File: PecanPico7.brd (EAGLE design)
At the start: 34.2 x 50 mm, 153 parts, among them IC1 Si4464-B1B-FM, IC10 TC1185-1.8VCT713, IC11 TC1185-2.5VCT713, IC12 ADR380ARTZ, IC13 RF6886, IC2 Si4464-B1B-FM, IC3 BME280_BME280, IC4 UBLOX_MAX-6, IC5 STM32F429IIH6, IC7 SPV1040, IC8 TXC_7Z, IC9 TPS62260DRVT, Q1 AP2301, Q2 AP2301, Q3 AP2301, U1 USD-SOCKETUSD, U2 PAC1720-1-AIA-TR, X1 CAMERA_HEADER

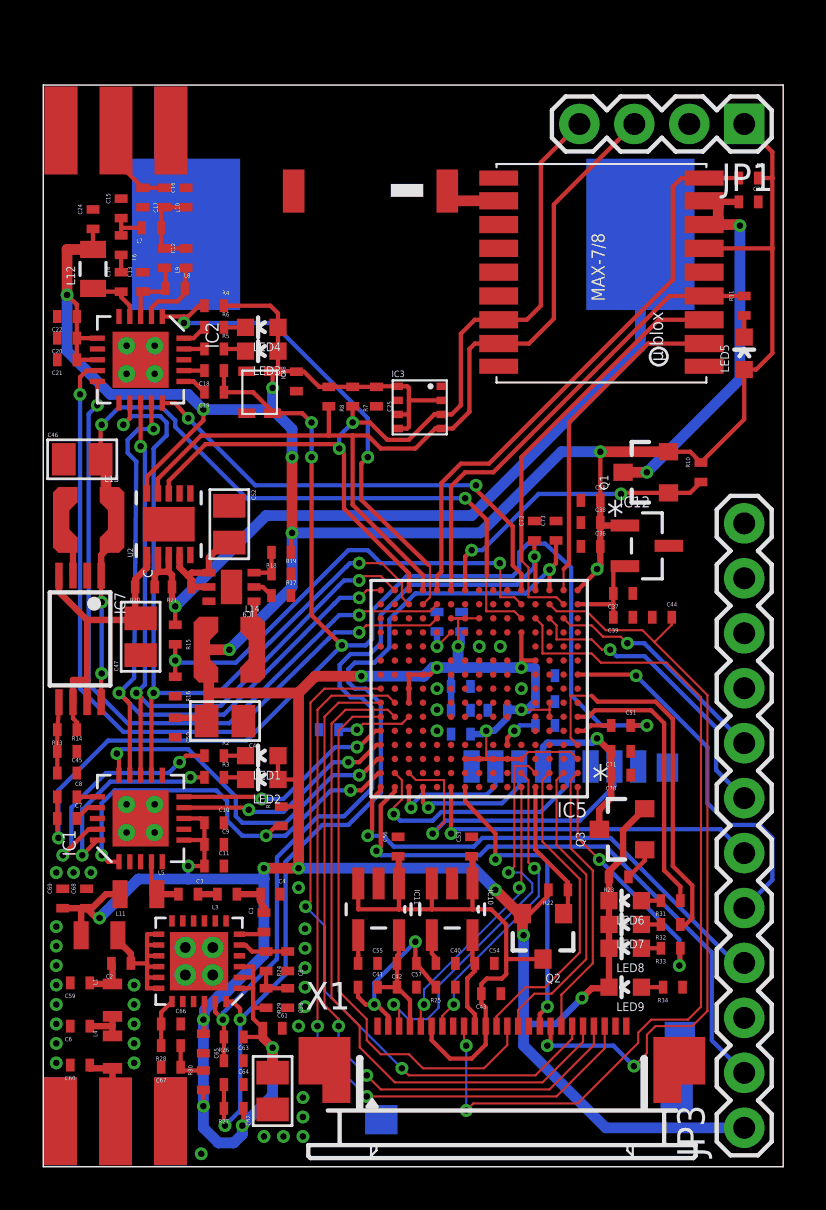
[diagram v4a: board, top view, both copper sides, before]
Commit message: Connected LED pins to pinheader
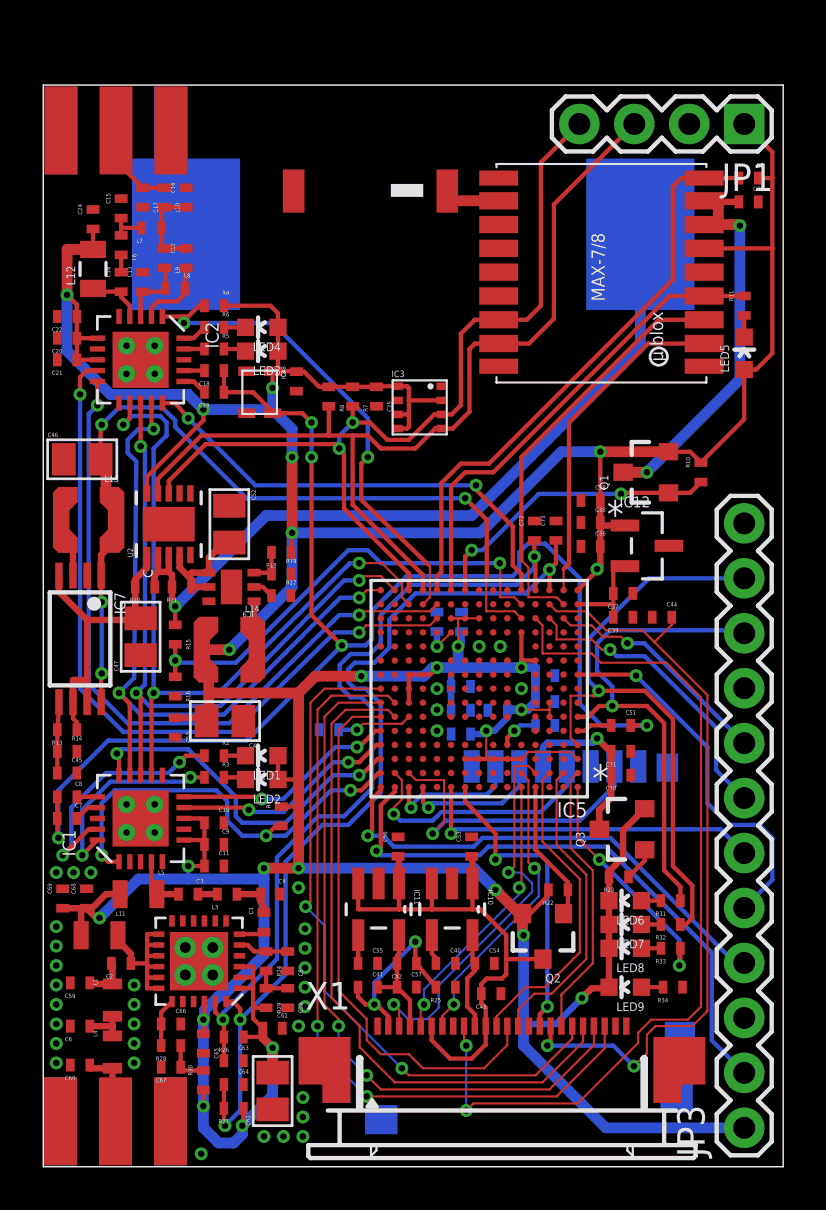
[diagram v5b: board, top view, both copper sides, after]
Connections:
- removed net N$45: JP3.10
- removed net N$46: JP3.11
- net LED1: now also JP3.10
- net LED2: now also JP3.11
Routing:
- net LED2: track 17.8 -> 29.0 mm, vias 0 -> 1
- net LED1: track 12.9 -> 23.3 mm, vias 0 -> 1
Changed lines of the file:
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@@
 <wire x1="15.2" y1="24.4" x2="14.9" y2="24.1" width="0.2" layer="16"/>
 <wire x1="14.9" y1="24.1" x2="13.8" y2="24.1" width="0.2" layer="16"/>
-<wire x1="23.2" y1="28.8" x2="24.4" y2="27.7" width="0.2" layer="16"/>
-<wire x1="24.4" y1="27.7" x2="24.4" y2="21.8" width="0.2" layer="16"/>
-<wire x1="24.4" y1="21.8" x2="25.8" y2="20.4" width="0.2" layer="16"/>
+<wire x1="23.2" y1="28.8" x2="24.8" y2="27.2" width="0.2" layer="16"/>
+<wire x1="24.8" y1="27.2" x2="24.8" y2="21.4" width="0.2" layer="16"/>
+<wire x1="24.8" y1="21.4" x2="25.8" y2="20.4" width="0.2" layer="16"/>
 <wire x1="25.8" y1="20.4" x2="27.9" y2="20.4" width="0.2" layer="16"/>
 <wire x1="27.15" y1="20.4" x2="27.9" y2="20.4" width="0.2" layer="1"/>
@@
 <contactref element="R24" pad="P$2"/>
 <contactref element="C5" pad="P$2"/>
-<wire x1="9.064" y1="10.25" x2="9.35" y2="10.25" width="0.2" layer="1"/>
-<wire x1="9.35" y1="10.25" x2="9.65" y2="9.95" width="0.2" layer="1"/>
-<wire x1="9.65" y1="9.95" x2="10.3" y2="9.95" width="0.2" layer="1"/>
+<wire x1="9.064" y1="10.25" x2="9.45" y2="10.25" width="0.2" layer="1"/>
+<wire x1="9.45" y1="10.25" x2="9.75" y2="9.95" width="0.2" layer="1"/>
+<wire x1="9.75" y1="9.95" x2="10.3" y2="9.95" width="0.2" layer="1"/>
 <wire x1="10.3" y1="9.95" x2="11.3" y2="9.95" width="0.2" layer="1"/>
 </signal>
@@
 <wire x1="21.2" y1="8.7" x2="21.4" y2="8.9" width="0.2" layer="1"/>
 <wire x1="21.4" y1="8.9" x2="21.4" y2="9.6" width="0.2" layer="1"/>
-<wire x1="21.4" y1="9.6" x2="21.4" y2="11.2" width="0.2" layer="1"/>
-<wire x1="21.4" y1="11.2" x2="20.7" y2="11.9" width="0.2" layer="1"/>
+<wire x1="21.4" y1="9.6" x2="21.4" y2="10.7" width="0.2" layer="1"/>
+<wire x1="21.4" y1="10.7" x2="20.2" y2="11.9" width="0.2" layer="1"/>
 <wire x1="14.5602" y1="13.0938" x2="14.5602" y2="11.9" width="0.2" layer="1"/>
 <wire x1="14.5602" y1="11.9" x2="16.4398" y2="11.9" width="0.2" layer="1"/>
 <wire x1="16.4398" y1="11.9" x2="17.9602" y2="11.9" width="0.2" layer="1"/>
 <wire x1="17.9602" y1="11.9" x2="19.8398" y2="11.9" width="0.2" layer="1"/>
-<wire x1="19.8398" y1="11.9" x2="20.7" y2="11.9" width="0.2" layer="1"/>
+<wire x1="19.8398" y1="11.9" x2="20.2" y2="11.9" width="0.2" layer="1"/>
 <wire x1="16.4398" y1="13.0938" x2="16.4398" y2="11.9" width="0.2" layer="1"/>
 <wire x1="17.9602" y1="13.0938" x2="17.9602" y2="11.9" width="0.2" layer="1"/>
@@
 <wire x1="27.8" y1="14.15" x2="27.8" y2="14.65" width="0.2" layer="1"/>
 </signal>
-<signal name="N$45">
-<contactref element="JP3" pad="10"/>
-</signal>
-<signal name="N$46">
-<contactref element="JP3" pad="11"/>
-</signal>
 <signal name="UART_TXD">
 <contactref element="IC5" pad="N3"/>
@@
 <wire x1="24.7" y1="19.5" x2="24.375" y2="19.825" width="0.1" layer="1"/>
 <wire x1="24.375" y1="19.825" x2="24.375" y2="21.775" width="0.1" layer="1"/>
-<wire x1="24.375" y1="21.775" x2="25.35" y2="21.775" width="0.1" layer="1"/>
-<wire x1="25.35" y1="21.775" x2="25.625" y2="21.5" width="0.2" layer="1"/>
-<wire x1="25.625" y1="21.5" x2="28.3" y2="21.5" width="0.2" layer="1"/>
-<wire x1="28.3" y1="21.5" x2="29.1" y2="20.7" width="0.2" layer="1"/>
+<wire x1="24.375" y1="21.775" x2="25.45" y2="21.775" width="0.1" layer="1"/>
+<wire x1="27.8" y1="22" x2="29.1" y2="20.7" width="0.2" layer="1"/>
 <wire x1="29.1" y1="20.7" x2="29.1" y2="13.9" width="0.2" layer="1"/>
 <wire x1="29.1" y1="13.9" x2="30" y2="13" width="0.2" layer="1"/>
@@
 <wire x1="30" y1="11.5" x2="29.7" y2="11.2" width="0.2" layer="1"/>
 <wire x1="29.7" y1="11.2" x2="29.45" y2="11.2" width="0.2" layer="1"/>
+<wire x1="25.675" y1="22" x2="25.45" y2="21.775" width="0.2" layer="1"/>
+<contactref element="JP3" pad="11"/>
+<via x="25.675" y="22" extent="1-16" drill="0.3"/>
+<wire x1="27.8" y1="22" x2="25.675" y2="22" width="0.2" layer="1"/>
+<wire x1="25.675" y1="22" x2="25.2" y2="22.475" width="0.2" layer="16"/>
+<wire x1="25.2" y1="22.475" x2="25.2" y2="24.4" width="0.2" layer="16"/>
+<wire x1="25.2" y1="24.4" x2="28" y2="27.2" width="0.2" layer="16"/>
+<wire x1="28" y1="27.2" x2="32.4" y2="27.2" width="0.2" layer="16"/>
 </signal>
 <signal name="LED1">
@@
 <contactref element="IC5" pad="F1"/>
 <wire x1="24.7" y1="20.8" x2="25.2" y2="20.8" width="0.2" layer="1"/>
-<wire x1="25.2" y1="20.8" x2="25.5" y2="21.1" width="0.2" layer="1"/>
-<wire x1="25.5" y1="21.1" x2="28.1" y2="21.1" width="0.2" layer="1"/>
-<wire x1="28.1" y1="21.1" x2="28.7" y2="20.5" width="0.2" layer="1"/>
+<wire x1="25.2" y1="20.8" x2="25.7" y2="21.3" width="0.2" layer="1"/>
+<wire x1="27.9" y1="21.3" x2="28.7" y2="20.5" width="0.2" layer="1"/>
 <wire x1="28.7" y1="20.5" x2="28.7" y2="13.7" width="0.2" layer="1"/>
 <wire x1="28.7" y1="13.7" x2="29.45" y2="12.95" width="0.2" layer="1"/>
 <wire x1="29.45" y1="12.95" x2="29.45" y2="12.3" width="0.2" layer="1"/>
+<contactref element="JP3" pad="10"/>
+<via x="26.3" y="21.3" extent="1-16" drill="0.3"/>
+<wire x1="25.7" y1="21.3" x2="26.3" y2="21.3" width="0.2" layer="1"/>
+<wire x1="27.9" y1="21.3" x2="26.3" y2="21.3" width="0.2" layer="1"/>
+<wire x1="26.3" y1="21.3" x2="26.3" y2="22.2" width="0.2" layer="16"/>
+<wire x1="26.3" y1="22.2" x2="25.6" y2="22.9" width="0.2" layer="16"/>
+<wire x1="25.6" y1="22.9" x2="25.6" y2="24.2" width="0.2" layer="16"/>
+<wire x1="25.6" y1="24.2" x2="26.2" y2="24.8" width="0.2" layer="16"/>
+<wire x1="26.2" y1="24.8" x2="32.26" y2="24.8" width="0.2" layer="16"/>
+<wire x1="32.26" y1="24.8" x2="32.4" y2="24.66" width="0.2" layer="16"/>
 </signal>
 <signal name="LED3">

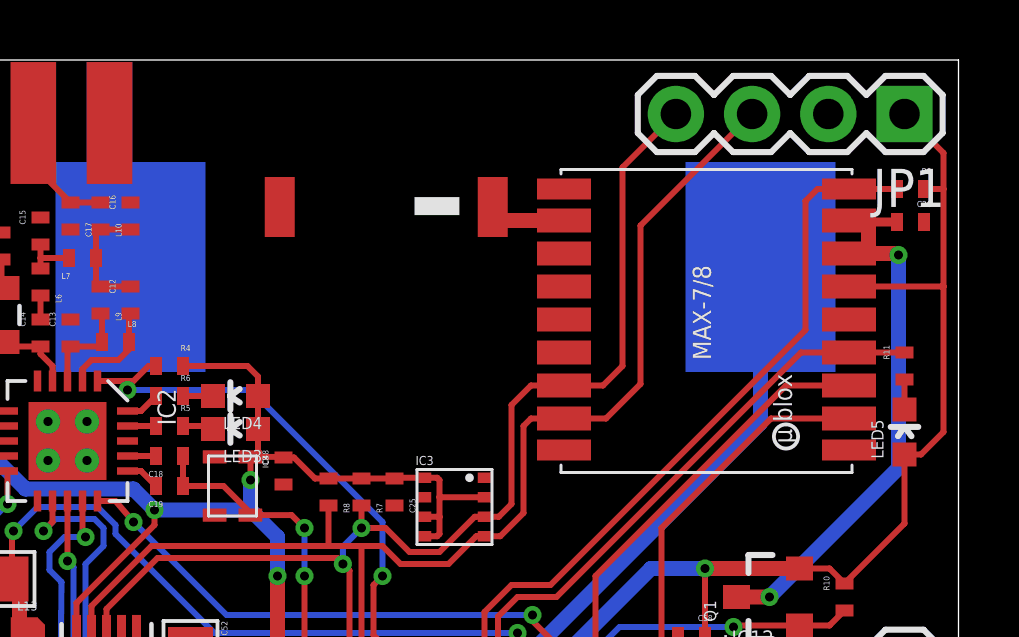
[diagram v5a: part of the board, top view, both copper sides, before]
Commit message: Added GPS preamplifier
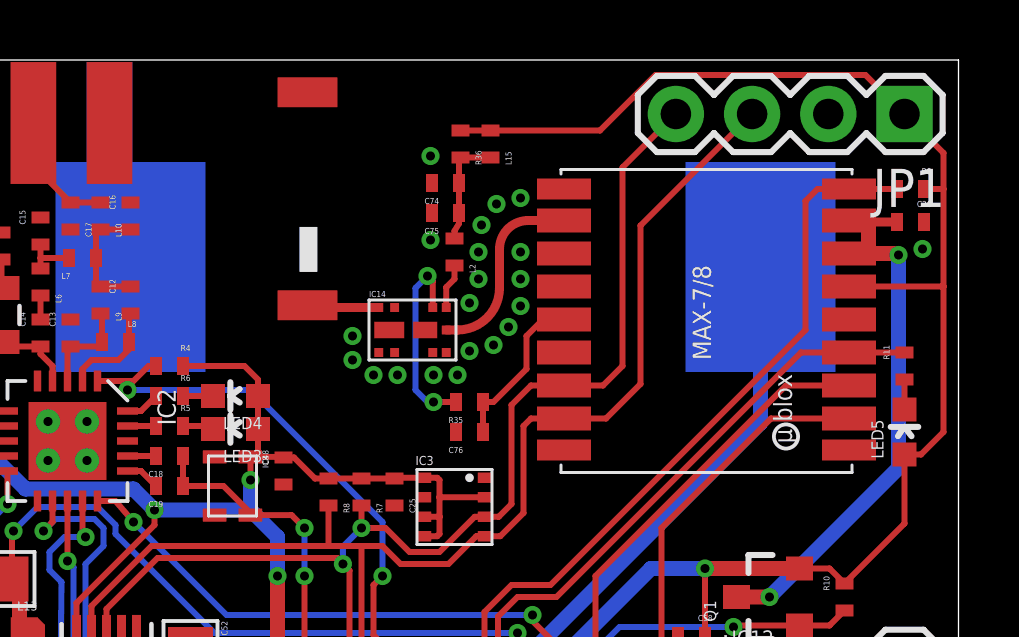
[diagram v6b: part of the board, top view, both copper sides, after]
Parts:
- added C74, C75, C76, L15, L2, R35, R36: (no value), PecanPico6:0402
- added IC14: ALM-GP003, stm32f42x:ALM-GP003
- C25: value 100pF -> 100nF
- R11: value 10k -> 3.3k
- moved U$4 3.00 mm to (12.5, 45.0), turned to 90 degrees
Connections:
- new net GPS_BIAS: C76.P$2, IC4.14_VCC_RF, R35.P$2
- new net N$45: IC14.8, R35.P$1
- new net N$46: IC14.7, L2.P$1
- new net N$51: C74.P$2, C75.P$2, L15.P$1, L2.P$2, R36.P$1
- new net N$7: IC14.1, U$4.FEED
- net GND: now also C74.P$1, C75.P$1, C76.P$1, IC14.2, IC14.3, IC14.4, IC14.9, IC14.P1, IC14.P2
- net N$33: now also IC14.6; no longer U$4.FEED
- net VCC: now also L15.P$2, R36.P$2
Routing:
- net VCC: track 268.2 -> 284.3 mm
- net N$45: track 0.00 -> 6.60 mm, vias 0 -> 2
- net GPS_BIAS: track 0.00 -> 5.48 mm
- net N$51: track 0.00 -> 3.79 mm
- net N$33: track 2.83 -> 6.20 mm
- net N$7: track 0.00 -> 2.45 mm
- net N$46: track 0.00 -> 1.51 mm

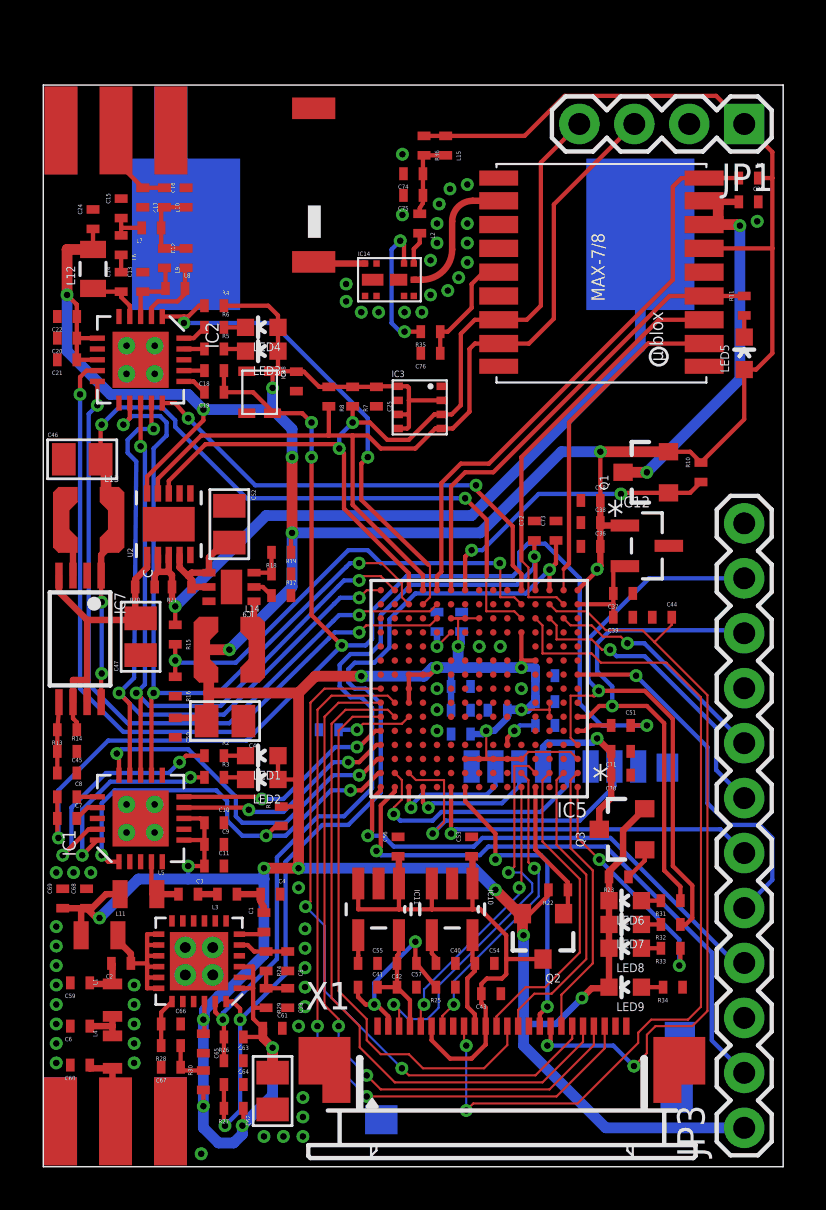
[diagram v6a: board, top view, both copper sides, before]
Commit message: Fixed impedance errors
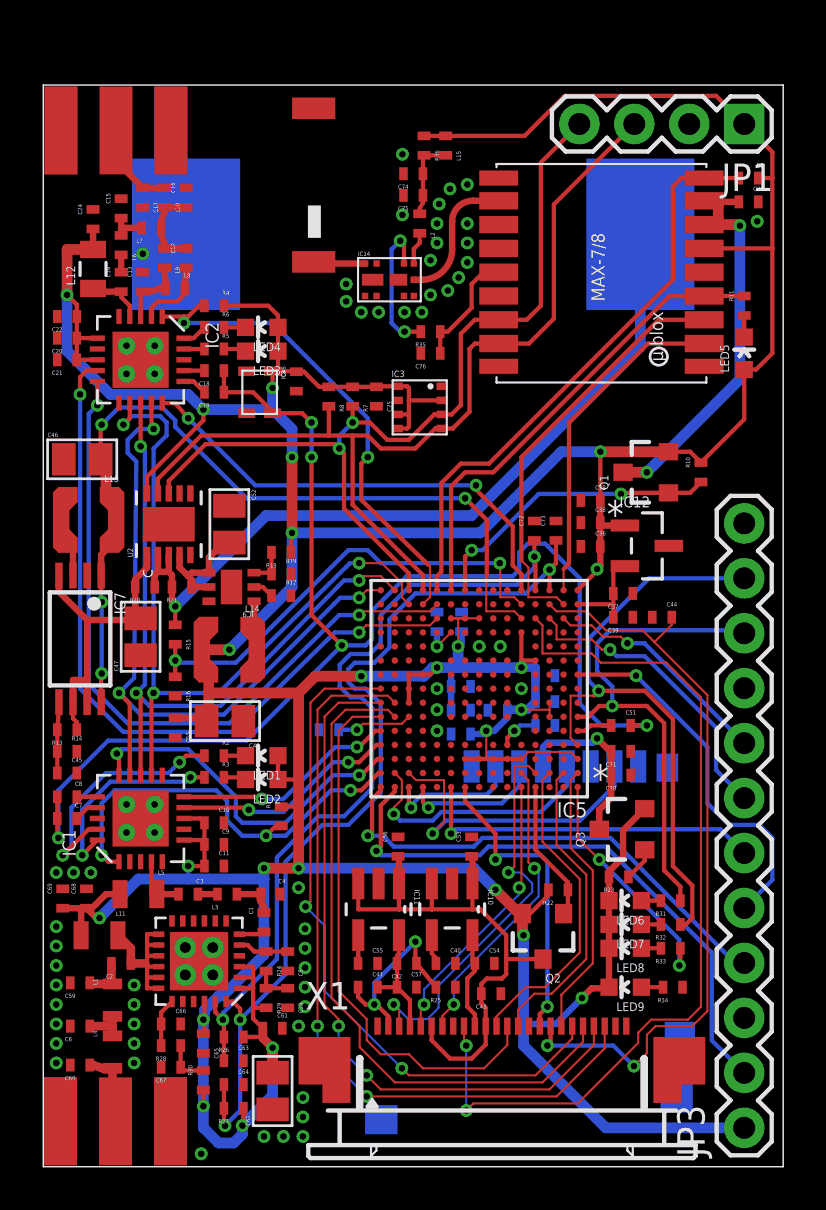
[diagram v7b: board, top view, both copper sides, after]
